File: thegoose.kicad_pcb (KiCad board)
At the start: 4 copper layers, 60 x 50 mm, 40 parts, among them U1 DRV8848, U2 DRV8848, U3 DRV8848, U4 AP64500SP-13

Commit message: Rework vias
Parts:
- removed ESP32: ESP32, hexy:ESP32
- C12, C5, C8: footprint Capacitor_SMD:C_0805_2012Metric -> Capacitor_SMD:C_0201_0603Metric
- C16: footprint Capacitor_SMD:C_0402_1005Metric -> Capacitor_SMD:C_0603_1608Metric
- moved C5 5.41 mm to (165.1, 92.3)
- moved BT1 2.06 mm to (172.5, 80.0)
- moved C8 1.49 mm to (166.1, 92.3)
- moved C12 0.74 mm to (164.1, 92.3)
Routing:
- net VCC: track 68.3 -> 70.7 mm
- net /ESP_D2: track 66.4 -> 67.6 mm
- net GND: track 41.7 -> 41.2 mm, vias 94 -> 19
- net /ESP_D13: vias 2 -> 1
- net (no net): vias 2 -> 0

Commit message: Goosification
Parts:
- added G***: LOGO, hexy:goose_logo, F.Cu at (131.2, 61.2)
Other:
- board text added: "THEGOOSE"

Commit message: Jark review
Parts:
- moved C8 13.6 mm to (156.5, 82.7), turned to 180 degrees
- moved C12 13.5 mm to (156.5, 81.1), turned to 180 degrees
- moved C5 13.5 mm to (156.5, 81.9), turned to 180 degrees
- turned L1 to 90 degrees
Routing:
- net VCC: track 70.7 -> 77.5 mm
- net /ESP_D2: track 67.6 -> 68.8 mm
- net GND: vias 19 -> 58

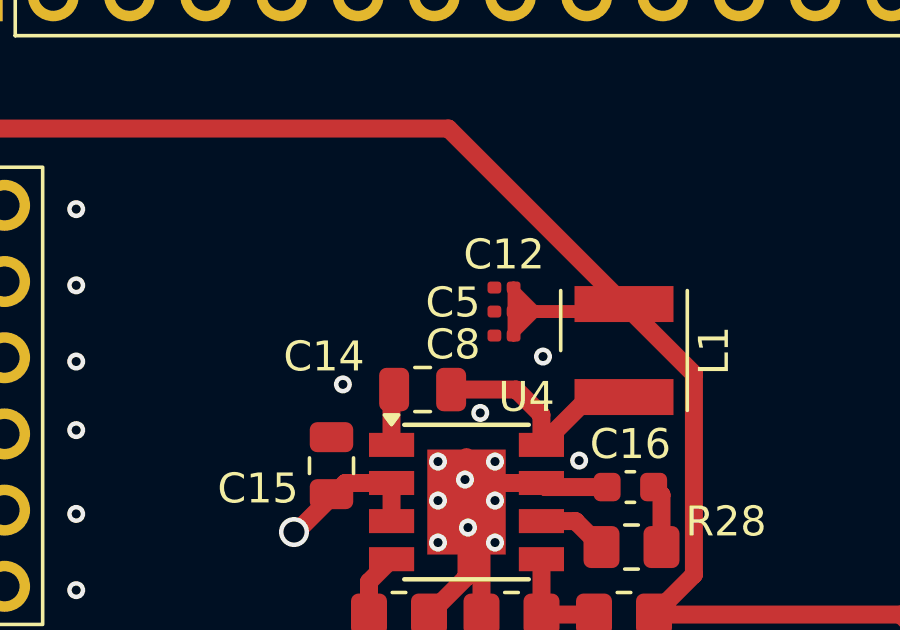
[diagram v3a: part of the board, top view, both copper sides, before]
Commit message: Update footprints
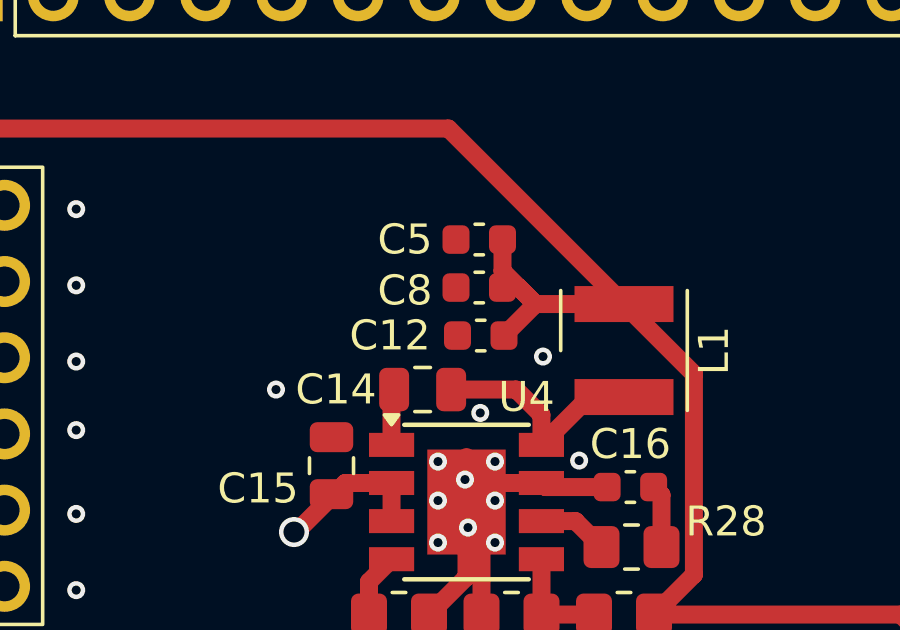
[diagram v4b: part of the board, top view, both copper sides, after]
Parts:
- C12, C5, C8: footprint Capacitor_SMD:C_0201_0603Metric -> Capacitor_SMD:C_0603_1608Metric
- moved C5 2.54 mm to (155.7, 79.5)
- moved C8 1.80 mm to (155.7, 81.1)
- moved C12 1.78 mm to (155.7, 82.7)
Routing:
- net VCC: track 77.5 -> 75.9 mm
